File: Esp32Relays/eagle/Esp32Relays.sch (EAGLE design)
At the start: 20 parts, among them J1 Audio2, J3 AUDIO_JACK_3.5MM_PTH, J4 AUDIO_JACK_3.5MM_PTH, U1 CD4066BE

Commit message: Changed cap values and some labels
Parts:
- removed C5: 2.2uF, SparkFun-Capacitors:2.2UF-0805-25V-(+80/-20%)
- removed J5: (no value), SparkFun-Connectors:CONN_03
- added AJ-IN: AUDIO_JACK_3.5MM_PTH, SparkFun-Connectors:AUDIO_JACK_3.5MM_PTH
- added C2: 1uF, SparkFun-Capacitors:2.2UF-0805-25V-(+80/-20%)
- C1, C3, C4: value 2.2uF -> 1uF
- J3: value AUDIO_JACK_3.5MM_PTH -> (none); device SparkFun-Connectors:AUDIO_JACK_3.5MM_PTH -> SparkFun-Connectors:CONN_03
- R3: value 4.7k -> 100k
- R4: value 100k -> 4.7k
- renumbered J4 to AJ-OUT
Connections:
- net 3V3: now also J3.2, R1.1; no longer J5.2, R3.1
- net A1-SIG-OUT: now also C3.2, R5.2; no longer C4.2, R6.2
- net A1IN: now also AJ-IN.RING, AJ-IN.RSH; no longer J3.RING, J3.RSH
- net A1OUT: now also C3.1; no longer C4.1
- net B1-SIG-IN: now also C2.2, R3.2; no longer C3.2, R4.2
- net B1-SIG-OUT: now also C4.2, R6.2; no longer C5.2, R5.2
- net B1IN: now also AJ-IN.TIP, AJ-IN.TSH, C2.1; no longer C3.1, J3.TIP, J3.TSH
- net B1OUT: now also C4.1; no longer C5.1
- net D26: now also J3.3; no longer J5.3
- net GND: now also AJ-IN.SLEEVE, J3.1, R4.2; no longer J3.SLEEVE, J5.1, R1.2
- net N$2: now also R1.2, R3.1; no longer R1.1, R3.2
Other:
- moved on the sheet: C3, C4, R1, R3, R4, R5, R6

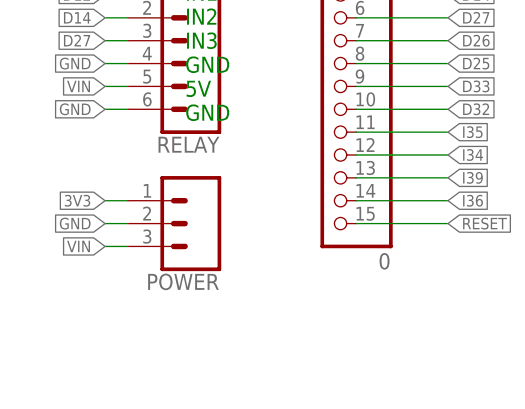
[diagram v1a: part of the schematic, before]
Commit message: Added brightness GPIO
and removed - unused - Touch IRQ pin
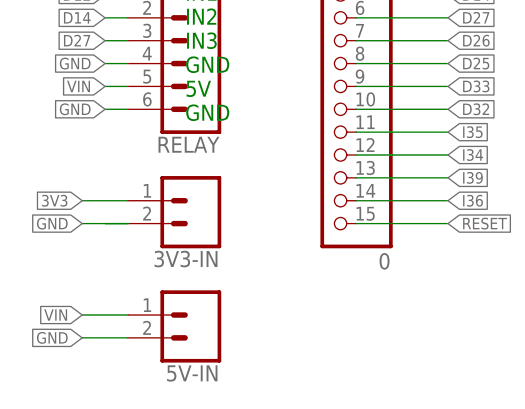
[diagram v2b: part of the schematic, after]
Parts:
- removed POWER: (no value), SparkFun-Connectors:CONN_03
- added 3V3-IN, 5V-IN: (no value), SparkFun-Connectors:CONN_02
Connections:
- net 3V3: now also 3V3-IN.1; no longer POWER.1
- net GND: now also 3V3-IN.2, 5V-IN.2; no longer POWER.2
- net VIN: now also 5V-IN.1; no longer POWER.3
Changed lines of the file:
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@@
 <?xml version="1.0" encoding="utf-8"?>
 <!DOCTYPE eagle SYSTEM "eagle.dtd">
-<eagle version="9.5.2">
+<eagle version="9.6.2">
 <drawing>
 <settings>
@@
 <part name="AJ-IN" library="SparkFun-Connectors" library_urn="urn:adsk.eagle:library:513" deviceset="AUDIO_JACK_3.5MM" device="_PTH" package3d_urn="urn:adsk.eagle:package:37997/1"/>
 <part name="AJ-OUT" library="SparkFun-Connectors" library_urn="urn:adsk.eagle:library:513" deviceset="AUDIO_JACK_3.5MM" device="_PTH" package3d_urn="urn:adsk.eagle:package:37997/1"/>
-<part name="POWER" library="SparkFun-Connectors" library_urn="urn:adsk.eagle:library:513" deviceset="CONN_03" device="" package3d_urn="urn:adsk.eagle:package:38063/1"/>
 <part name="J1" library="SparkFun-Connectors" library_urn="urn:adsk.eagle:library:513" deviceset="CONN_03X2" device="FEMALE" package3d_urn="urn:adsk.eagle:package:38016/1" value="Audio2"/>
 <part name="R4" library="SparkFun-Resistors" deviceset="0.3OHM" device="-0805-1/8W-1%" value="4.7k"/>
@@
 <part name="J2" library="SparkFun-Connectors" library_urn="urn:adsk.eagle:library:513" deviceset="CONN_03" device="" package3d_urn="urn:adsk.eagle:package:38063/1"/>
 <part name="J3" library="SparkFun-Connectors" library_urn="urn:adsk.eagle:library:513" deviceset="CONN_03" device="" package3d_urn="urn:adsk.eagle:package:38063/1"/>
+<part name="3V3-IN" library="SparkFun-Connectors" library_urn="urn:adsk.eagle:library:513" deviceset="CONN_02" device="" package3d_urn="urn:adsk.eagle:package:38039/1"/>
+<part name="5V-IN" library="SparkFun-Connectors" library_urn="urn:adsk.eagle:library:513" deviceset="CONN_02" device="" package3d_urn="urn:adsk.eagle:package:38039/1"/>
 </parts>
 <sheets>
@@
 <attribute name="VALUE" x="99.06" y="114.3" size="1.778" layer="96" font="vector"/>
 </instance>
-<instance part="POWER" gate="J$1" x="27.94" y="66.04" smashed="yes" rot="R180">
-<attribute name="VALUE" x="30.48" y="73.406" size="1.778" layer="96" font="vector" rot="R180"/>
-<attribute name="NAME" x="30.48" y="60.452" size="1.778" layer="95" font="vector" rot="R180"/>
-</instance>
 <instance part="J1" gate="G$1" x="30.48" y="121.92" smashed="yes">
 <attribute name="NAME" x="26.924" y="127.508" size="1.778" layer="95" font="vector"/>
@@
 <attribute name="VALUE" x="33.02" y="154.686" size="1.778" layer="96" font="vector" rot="R180"/>
 <attribute name="NAME" x="33.02" y="141.732" size="1.778" layer="95" font="vector" rot="R180"/>
+</instance>
+<instance part="3V3-IN" gate="G$1" x="27.94" y="68.58" smashed="yes" rot="R180">
+<attribute name="VALUE" x="30.48" y="73.406" size="1.778" layer="96" font="vector" rot="R180"/>
+<attribute name="NAME" x="30.48" y="62.992" size="1.778" layer="95" font="vector" rot="R180"/>
+</instance>
+<instance part="5V-IN" gate="G$1" x="27.94" y="55.88" smashed="yes" rot="R180">
+<attribute name="VALUE" x="30.48" y="60.706" size="1.778" layer="96" font="vector" rot="R180"/>
+<attribute name="NAME" x="30.48" y="50.292" size="1.778" layer="95" font="vector" rot="R180"/>
 </instance>
 </instances>
@@
 </segment>
 <segment>
-<pinref part="POWER" gate="J$1" pin="3"/>
-<wire x1="20.32" y1="63.5" x2="17.78" y2="63.5" width="0.1524" layer="91"/>
-<label x="17.78" y="63.5" size="1.27" layer="95" rot="R180" xref="yes"/>
-</segment>
-<segment>
 <pinref part="RELAY" gate="G$1" pin="5"/>
 <wire x1="20.32" y1="81.28" x2="17.78" y2="81.28" width="0.1524" layer="91"/>
 <label x="17.78" y="81.28" size="1.27" layer="95" rot="R180" xref="yes"/>
 </segment>
+<segment>
+<pinref part="5V-IN" gate="G$1" pin="1"/>
+<wire x1="20.32" y1="55.88" x2="15.24" y2="55.88" width="0.1524" layer="91"/>
+<label x="15.24" y="55.88" size="1.27" layer="95" rot="R180" xref="yes"/>
+</segment>
 </net>
 <net name="GND" class="1">
@@
 </segment>
 <segment>
-<pinref part="POWER" gate="J$1" pin="2"/>
 <wire x1="20.32" y1="66.04" x2="17.78" y2="66.04" width="0.1524" layer="91"/>
-<label x="17.78" y="66.04" size="1.27" layer="95" rot="R180" xref="yes"/>
+<pinref part="3V3-IN" gate="G$1" pin="2"/>
+<wire x1="20.32" y1="66.04" x2="15.24" y2="66.04" width="0.1524" layer="91"/>
+<label x="15.24" y="66.04" size="1.27" layer="95" rot="R180" xref="yes"/>
 </segment>
 <segment>
@@
 <label x="20.32" y="149.86" size="1.27" layer="95" rot="R180" xref="yes"/>
 </segment>
+<segment>
+<pinref part="5V-IN" gate="G$1" pin="2"/>
+<wire x1="20.32" y1="53.34" x2="15.24" y2="53.34" width="0.1524" layer="91"/>
+<label x="15.24" y="53.34" size="1.27" layer="95" rot="R180" xref="yes"/>
+</segment>
 </net>
 <net name="D13" class="0">
@@
 </segment>
 <segment>
-<pinref part="POWER" gate="J$1" pin="1"/>
-<wire x1="20.32" y1="68.58" x2="17.78" y2="68.58" width="0.1524" layer="91"/>
-<label x="17.78" y="68.58" size="1.27" layer="95" rot="R180" xref="yes"/>
-</segment>
-<segment>
 <pinref part="R1" gate="G$1" pin="1"/>
 <wire x1="48.26" y1="154.94" x2="45.72" y2="154.94" width="0.1524" layer="91"/>
@@
 <label x="20.32" y="147.32" size="1.27" layer="95" rot="R180" xref="yes"/>
 </segment>
-</net>
+<segment>
+<pinref part="3V3-IN" gate="G$1" pin="1"/>
+<wire x1="20.32" y1="68.58" x2="15.24" y2="68.58" width="0.1524" layer="91"/>
+<label x="15.24" y="68.58" size="1.27" layer="95" rot="R180" xref="yes"/>
+</segment>
+</net>
